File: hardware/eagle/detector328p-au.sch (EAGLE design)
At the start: 66 parts, among them K1 SRD-05VDC-SL-C, Q1 BSS123, Q2 16MHz, T1 BC817, T2 BC817, T3 BC817, U1 ATMEGA328P-AU

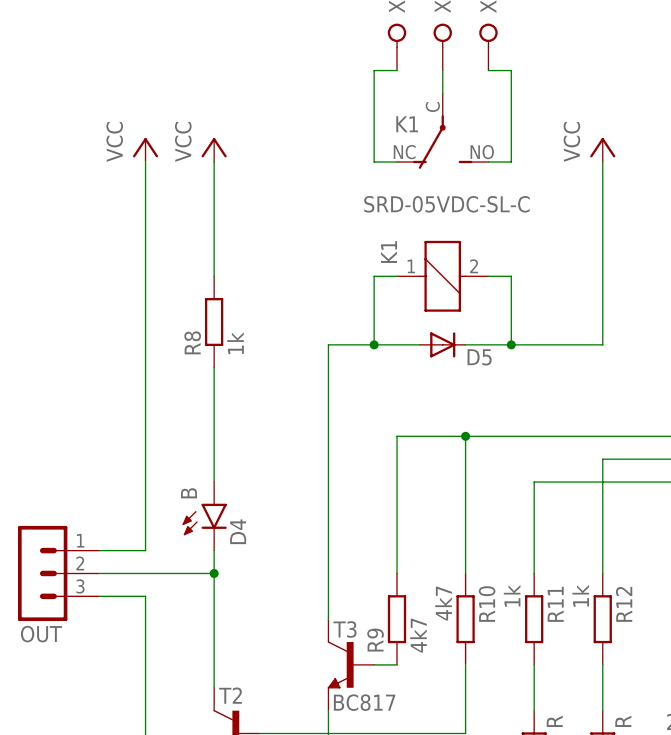
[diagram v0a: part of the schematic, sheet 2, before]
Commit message: detector_t85-pu: T2 10K pull-up, Zener 5,1V -> 20V
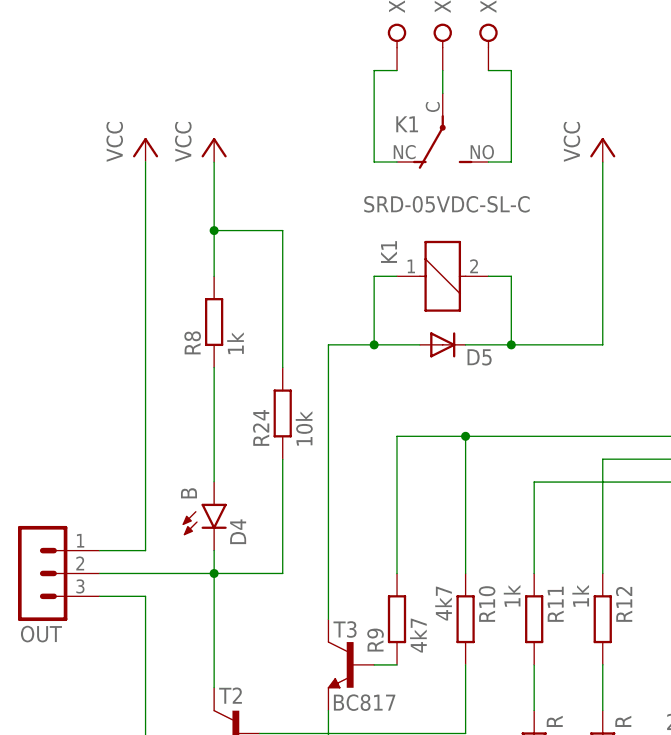
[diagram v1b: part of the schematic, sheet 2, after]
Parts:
- added R24: 10k, resistor:R-EU_R0603
- D1, D2: value 5.1V 0.5W -> 20V 0.5W
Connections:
- net N$23: now also R24.1
- net VCC: now also R24.2
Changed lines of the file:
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@@
 <part name="R4" library="resistor" deviceset="R-EU_" device="R0603" value="150"/>
 <part name="GND6" library="supply1" deviceset="GND" device=""/>
-<part name="D1" library="diode" deviceset="ZENER-DIODE" device="SOD80C" value="5.1V 0.5W"/>
-<part name="D2" library="diode" deviceset="ZENER-DIODE" device="SOD80C" value="5.1V 0.5W"/>
+<part name="D1" library="diode" deviceset="ZENER-DIODE" device="SOD80C" value="20V 0.5W"/>
+<part name="D2" library="diode" deviceset="ZENER-DIODE" device="SOD80C" value="20V 0.5W"/>
 <part name="GND-ISO1" library="SparkFun-Aesthetics" deviceset="GND-ISO" device=""/>
 <part name="R1" library="resistor" deviceset="R-EU_" device="R0603" value="1M8"/>
@@
 <part name="POWER" library="con-lstb" deviceset="MA03-2" device=""/>
 <part name="SERIAL" library="con-lstb" deviceset="MA03-1" device=""/>
+<part name="R24" library="resistor" deviceset="R-EU_" device="R0603" value="10k"/>
 </parts>
 <sheets>
@@
 <instance part="LCD" gate="1" x="198.12" y="66.04" rot="R180"/>
 <instance part="SERIAL" gate="G$1" x="198.12" y="53.34" rot="R180"/>
+<instance part="R24" gate="G$1" x="25.4" y="55.88" smashed="yes" rot="R90">
+<attribute name="NAME" x="23.9014" y="52.07" size="1.778" layer="95" rot="R90"/>
+<attribute name="VALUE" x="28.702" y="52.07" size="1.778" layer="96" rot="R90"/>
+</instance>
 </instances>
 <busses>
@@
 <pinref part="R8" gate="G$1" pin="2"/>
 <pinref part="P+5" gate="VCC" pin="VCC"/>
-<wire x1="17.78" y1="71.12" x2="17.78" y2="83.82" width="0.1524" layer="91"/>
+<wire x1="17.78" y1="71.12" x2="17.78" y2="76.2" width="0.1524" layer="91"/>
+<pinref part="R24" gate="G$1" pin="2"/>
+<wire x1="17.78" y1="76.2" x2="17.78" y2="83.82" width="0.1524" layer="91"/>
+<wire x1="25.4" y1="60.96" x2="25.4" y2="76.2" width="0.1524" layer="91"/>
+<wire x1="25.4" y1="76.2" x2="17.78" y2="76.2" width="0.1524" layer="91"/>
+<junction x="17.78" y="76.2"/>
 </segment>
 <segment>
@@
 <wire x1="5.08" y1="38.1" x2="17.78" y2="38.1" width="0.1524" layer="91"/>
 <junction x="17.78" y="38.1"/>
-</segment>
-</net>
+<pinref part="R24" gate="G$1" pin="1"/>
+<wire x1="25.4" y1="50.8" x2="25.4" y2="38.1" width="0.1524" layer="91"/>
+<wire x1="25.4" y1="38.1" x2="17.78" y2="38.1" width="0.1524" layer="91"/>
+</segment>
+</net>
